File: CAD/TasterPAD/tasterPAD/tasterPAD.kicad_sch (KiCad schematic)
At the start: 28 parts, among them J1 Conn_01x04_Pin, J2 Conn_01x17_Pin, J3 SPI Programmer IF, U1 74HC165, U2 74HC165, U3 ATtiny13A-P

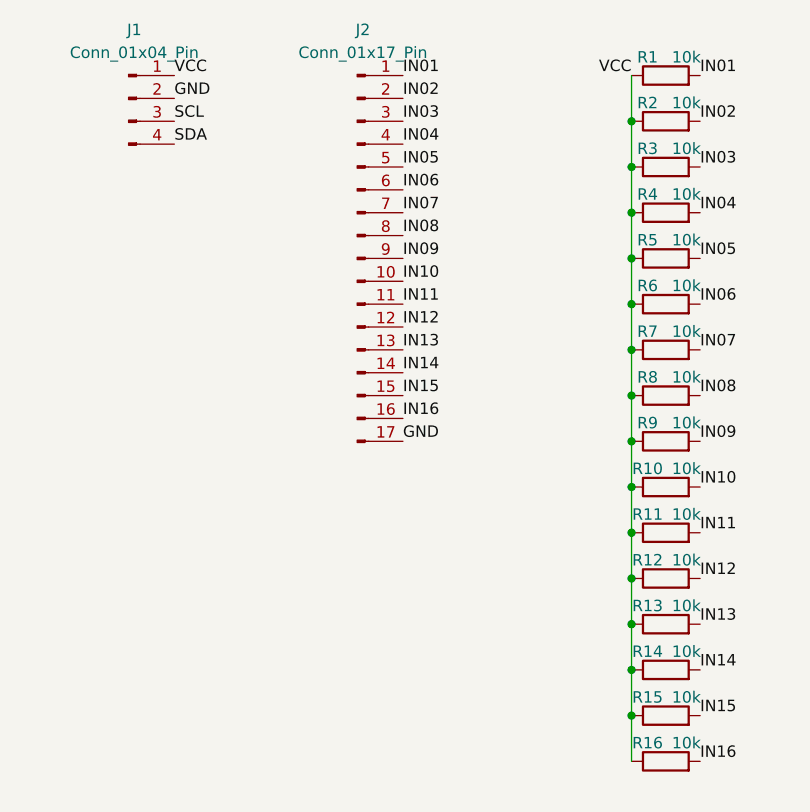
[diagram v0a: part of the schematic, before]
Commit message: updated Taster PCB
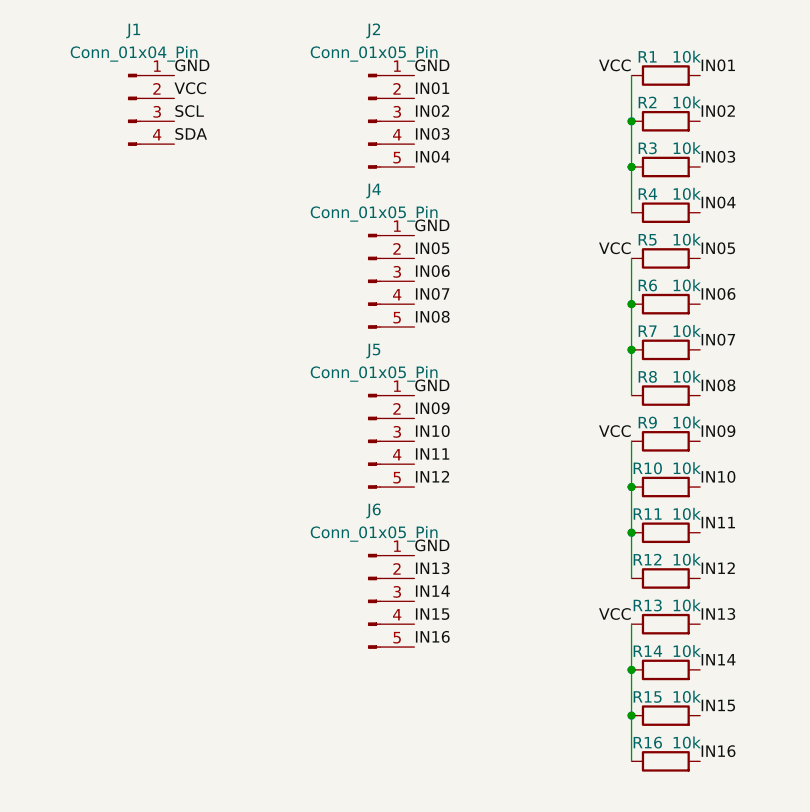
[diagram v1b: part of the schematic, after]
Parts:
- removed J2: Conn_01x17_Pin, Connector_PinHeader_2.54mm:PinHeader_1x17_P2.54mm_Vertical, symbol Connector:Conn_01x17_Pin
- added J2, J4, J5, J6: Conn_01x05_Pin, Connector_PinHeader_2.54mm:PinHeader_1x05_P2.54mm_Vertical, symbol Connector:Conn_01x05_Pin
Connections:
- net GND: now also J1.1 (Pin_1), J2.1 (Pin_1), J4.1 (Pin_1), J5.1 (Pin_1), J6.1 (Pin_1); no longer J1.2 (Pin_2)
- net IN01: now also J2.2 (Pin_2)
- net IN02: now also J2.3 (Pin_3)
- net IN03: now also J2.4 (Pin_4)
- net IN04: now also J2.5 (Pin_5)
- net IN05: now also J4.2 (Pin_2)
- net IN06: now also J4.3 (Pin_3)
- net IN07: now also J4.4 (Pin_4)
- net IN08: now also J4.5 (Pin_5)
- net IN09: now also J5.2 (Pin_2)
- net IN10: now also J5.3 (Pin_3)
- net IN11: now also J5.4 (Pin_4)
- net IN12: now also J5.5 (Pin_5)
- net IN13: now also J6.2 (Pin_2)
- net IN14: now also J6.3 (Pin_3)
- net IN15: now also J6.4 (Pin_4)
- net IN16: now also J6.5 (Pin_5)
- net VCC: now also J1.2 (Pin_2); no longer J1.1 (Pin_1)
